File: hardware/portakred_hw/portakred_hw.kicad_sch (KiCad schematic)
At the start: 24 parts, among them J1 USB_C_Receptacle_USB2.0_16P, J2 DISPLAY, Q1 BC847, SW13 RESET, SW14 BOOT, U2 TLV75533PDBV, U3 USBLC6-2SC6, U4 ESP32-S3-WROOM-2

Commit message: Fix buzzer connection, fix keypad diodes and add description, move NFC antenna wire to be pretty :)
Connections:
- net +5V: now also BZ1.1 (+); no longer Q1.3 (C)
- net GND: now also Q1.2 (E); no longer BZ1.2 (-)
- new net: BZ1.2 (-), Q1.3 (C)
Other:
- moved on the sheet: BZ1, Q1
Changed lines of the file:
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@@
+    (stroke (width 0) (type default))
+  )
+  (wire (pts (xy 261.62 191.77) (xy 261.62 185.42))
     (stroke (width 0) (type default))
   )
@@
     (stroke (width 0) (type default))
   )
-  (wire (pts (xy 259.08 182.88) (xy 261.62 182.88))
-    (stroke (width 0) (type default))
-  )
   (wire (pts (xy 317.5 135.89) (xy 317.5 148.59))
     (stroke (width 0) (type default))
@@
     (stroke (width 0) (type default))
   )
-  (wire (pts (xy 254 170.18) (xy 250.19 170.18))
-    (stroke (width 0) (type default))
-  )
   (wire (pts (xy 290.83 135.89) (xy 290.83 115.57))
     (stroke (width 0) (type default))
@@
     (stroke (width 0) (type default))
   )
-  (wire (pts (xy 261.62 177.8) (xy 261.62 175.26))
-    (stroke (width 0) (type default))
-  )
   (wire (pts (xy 83.82 72.39) (xy 83.82 78.74))
     (stroke (width 0) (type default))
@@
     (stroke (width 0) (type default))
   )
+  (wire (pts (xy 254 180.34) (xy 250.19 180.34))
+    (stroke (width 0) (type default))
+  )
   (wire (pts (xy 247.65 72.39) (xy 247.65 118.11))
     (stroke (width 0) (type default))
@@
     (stroke (width 0) (type default))
   )
+  (wire (pts (xy 261.62 163.83) (xy 261.62 166.37))
+    (stroke (width 0) (type default))
+  )
   (wire (pts (xy 251.46 93.98) (xy 251.46 123.19))
     (stroke (width 0) (type default))
@@
     (stroke (width 0) (type default))
   )
-  (wire (pts (xy 261.62 163.83) (xy 261.62 165.1))
+  (wire (pts (xy 261.62 171.45) (xy 261.62 175.26))
     (stroke (width 0) (type default))
   )
@@
     (stroke (width 0) (type default))
   )
-  (wire (pts (xy 250.19 170.18) (xy 250.19 166.37))
+  (wire (pts (xy 250.19 166.37) (xy 250.19 180.34))
     (stroke (width 0) (type default))
   )
@@
     )
   )
-  (symbol (lib_id "Device:Buzzer") (at 264.16 180.34 0) (unit 1)
-    (in_bom yes) (on_board yes) (dnp no) (fields_autoplaced)
-    (property "Reference" "BZ1" (at 267.97 179.07 0)
-      (effects (font (size 1.27 1.27)) (justify left))
-    )
-    (property "Value" "Buzzer" (at 267.97 181.61 0)
-      (effects (font (size 1.27 1.27)) (justify left))
-    )
-    (property "Footprint" "Buzzer_Beeper:Buzzer_15x7.5RM7.6" (at 263.525 177.8 90)
-      (effects (font (size 1.27 1.27)) hide)
-    )
-    (property "Datasheet" "~" (at 263.525 177.8 90)
+  (symbol (lib_id "Device:Buzzer") (at 264.16 168.91 0) (unit 1)
+    (in_bom yes) (on_board yes) (dnp no) (fields_autoplaced)
+    (property "Reference" "BZ1" (at 267.97 167.64 0)
+      (effects (font (size 1.27 1.27)) (justify left))
+    )
+    (property "Value" "Buzzer" (at 267.97 170.18 0)
+      (effects (font (size 1.27 1.27)) (justify left))
+    )
+    (property "Footprint" "Buzzer_Beeper:Buzzer_15x7.5RM7.6" (at 263.525 166.37 90)
+      (effects (font (size 1.27 1.27)) hide)
+    )
+    (property "Datasheet" "~" (at 263.525 166.37 90)
       (effects (font (size 1.27 1.27)) hide)
     )
@@
     )
   )
-  (symbol (lib_id "power:GND") (at 259.08 182.88 0) (unit 1)
-    (in_bom yes) (on_board yes) (dnp no) (fields_autoplaced)
-    (property "Reference" "#PWR035" (at 259.08 189.23 0)
-      (effects (font (size 1.27 1.27)) hide)
-    )
-    (property "Value" "GND" (at 259.08 187.96 0)
-      (effects (font (size 1.27 1.27)))
-    )
-    (property "Footprint" "" (at 259.08 182.88 0)
-      (effects (font (size 1.27 1.27)) hide)
-    )
-    (property "Datasheet" "" (at 259.08 182.88 0)
+  (symbol (lib_id "power:GND") (at 261.62 191.77 0) (unit 1)
+    (in_bom yes) (on_board yes) (dnp no) (fields_autoplaced)
+    (property "Reference" "#PWR035" (at 261.62 198.12 0)
+      (effects (font (size 1.27 1.27)) hide)
+    )
+    (property "Value" "GND" (at 261.62 196.85 0)
+      (effects (font (size 1.27 1.27)))
+    )
+    (property "Footprint" "" (at 261.62 191.77 0)
+      (effects (font (size 1.27 1.27)) hide)
+    )
+    (property "Datasheet" "" (at 261.62 191.77 0)
       (effects (font (size 1.27 1.27)) hide)
     )
@@
     )
   )
-  (symbol (lib_id "Transistor_BJT:BC847") (at 259.08 170.18 0) (unit 1)
-    (in_bom yes) (on_board yes) (dnp no) (fields_autoplaced)
-    (property "Reference" "Q1" (at 264.16 168.91 0)
-      (effects (font (size 1.27 1.27)) (justify left))
-    )
-    (property "Value" "BC847" (at 264.16 171.45 0)
-      (effects (font (size 1.27 1.27)) (justify left))
-    )
-    (property "Footprint" "Package_TO_SOT_SMD:SOT-23" (at 264.16 172.085 0)
+  (symbol (lib_id "Transistor_BJT:BC847") (at 259.08 180.34 0) (unit 1)
+    (in_bom yes) (on_board yes) (dnp no) (fields_autoplaced)
+    (property "Reference" "Q1" (at 264.16 179.07 0)
+      (effects (font (size 1.27 1.27)) (justify left))
+    )
+    (property "Value" "BC847" (at 264.16 181.61 0)
+      (effects (font (size 1.27 1.27)) (justify left))
+    )
+    (property "Footprint" "Package_TO_SOT_SMD:SOT-23" (at 264.16 182.245 0)
       (effects (font (size 1.27 1.27) italic) (justify left) hide)
     )
-    (property "Datasheet" "http://www.infineon.com/dgdl/Infineon-BC847SERIES_BC848SERIES_BC849SERIES_BC850SERIES-DS-v01_01-en.pdf?fileId=db3a304314dca389011541d4630a1657" (at 259.08 170.18 0)
+    (property "Datasheet" "http://www.infineon.com/dgdl/Infineon-BC847SERIES_BC848SERIES_BC849SERIES_BC850SERIES-DS-v01_01-en.pdf?fileId=db3a304314dca389011541d4630a1657" (at 259.08 180.34 0)
       (effects (font (size 1.27 1.27)) (justify left) hide)
     )

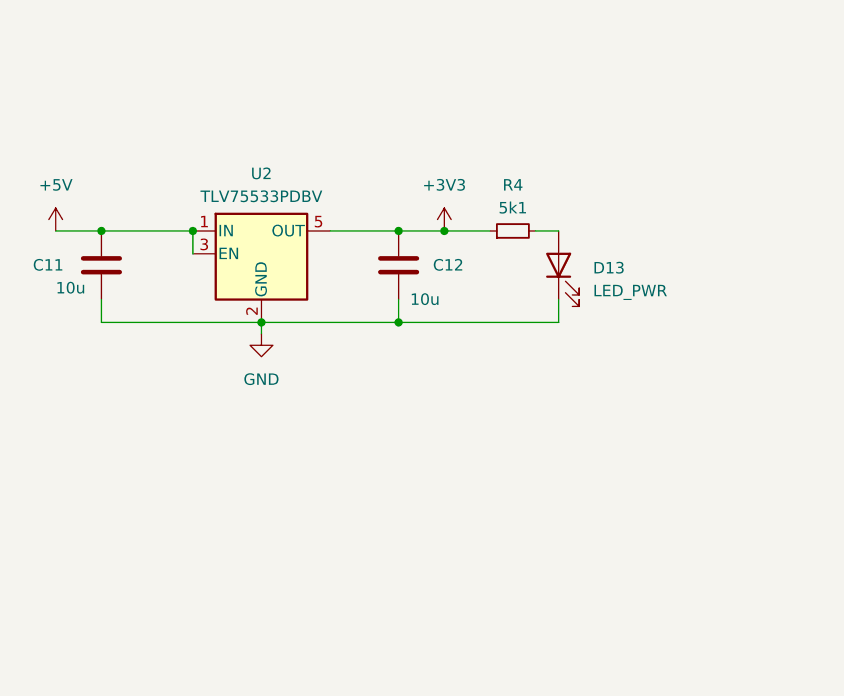
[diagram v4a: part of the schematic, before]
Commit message: Added battery holder from JLCPCB library, created new sheet for battery subsystem, upadted README
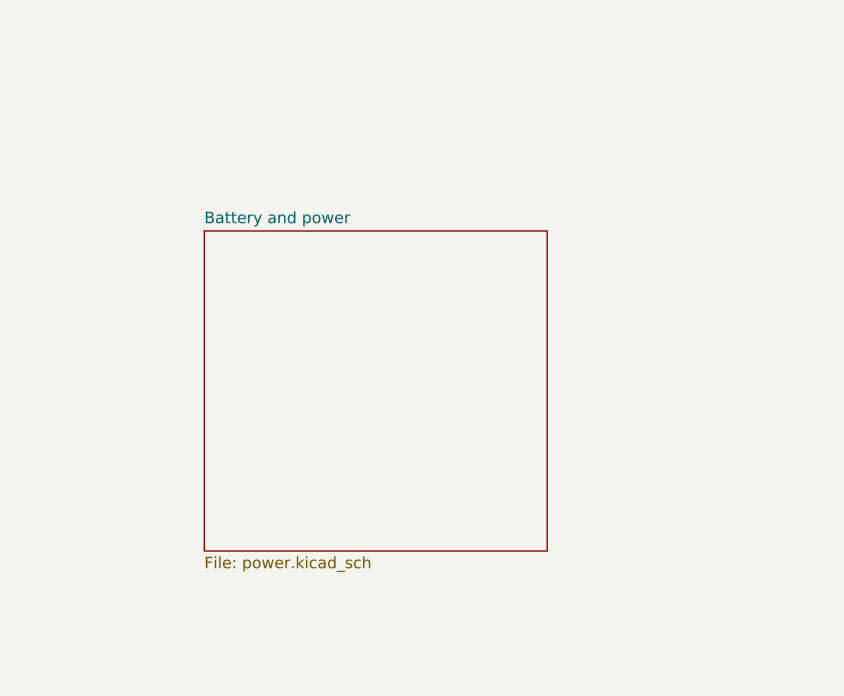
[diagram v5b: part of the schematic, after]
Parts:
- removed C11, C12: 10u, symbol Device:C
- removed D13: LED_PWR, symbol Device:LED
- removed R4: 5k1, symbol Device:R_Small
- removed U2: TLV75533PDBV, Package_TO_SOT_SMD:SOT-23-5, symbol Regulator_Linear:TLV75533PDBV
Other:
- added sheet Battery and power (power.kicad_sch)
